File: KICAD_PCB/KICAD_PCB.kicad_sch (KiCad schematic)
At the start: 6 parts, among them J1 RPi, J2 Protoboard, U1 TPS7A0233DBVR

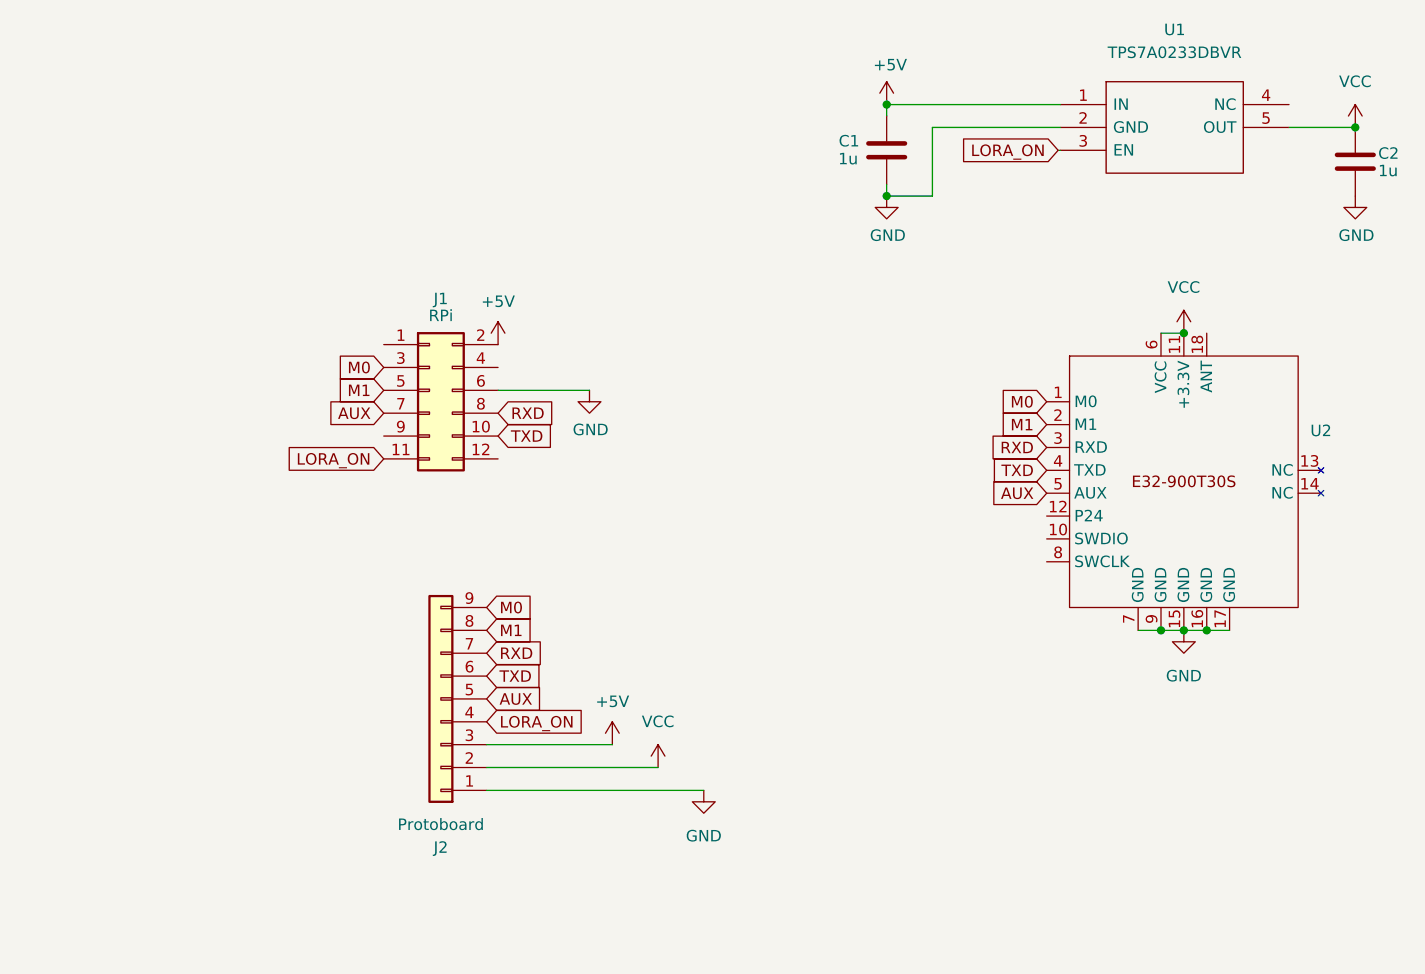
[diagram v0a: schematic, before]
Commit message: Adição do conector genérico J3
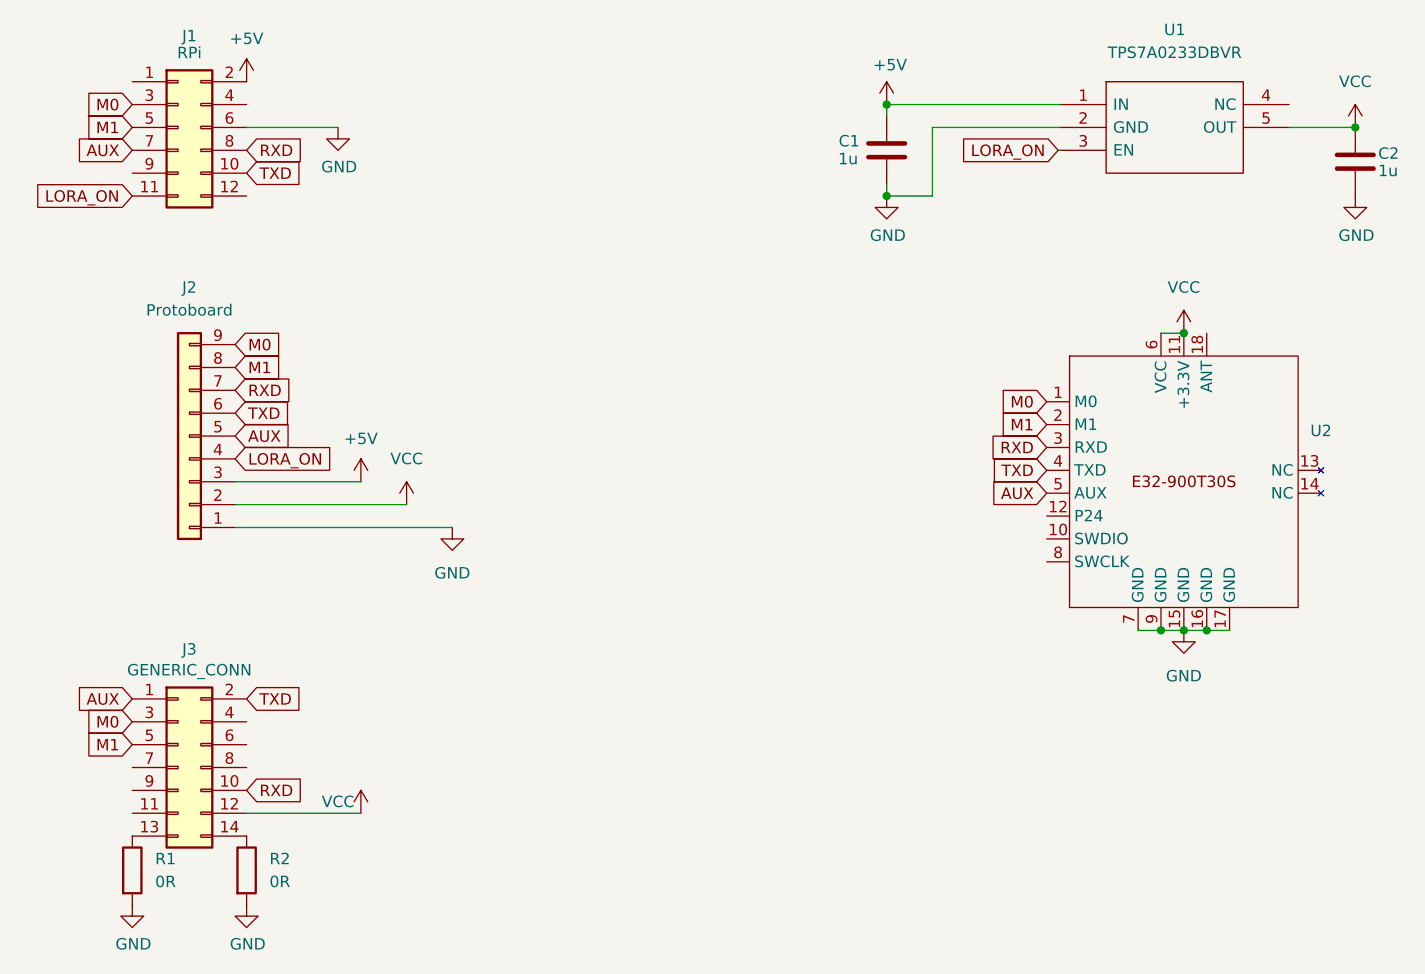
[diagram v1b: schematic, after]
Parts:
- added J3: GENERIC_CONN, Connector_PinSocket_2.54mm:PinSocket_2x07_P2.54mm_Vertical, symbol MICRO-SOP_RADIO-GENERIC-rescue:Conn_02x07_Odd_Even-Connector_Generic
- added R1, R2: 0R, Resistor_SMD:R_0805_2012Metric, symbol Device:R
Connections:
- net AUX: now also J3.1 (Pin_1)
- net GND: now also R1.2, R2.2
- net M0: now also J3.3 (Pin_3)
- net M1: now also J3.5 (Pin_5)
- net RXD: now also J3.10 (Pin_10)
- net TXD: now also J3.2 (Pin_2)
- net VCC: now also J3.12 (Pin_12)
- new net: J3.14 (Pin_14), R2.1
- new net: J3.13 (Pin_13), R1.1
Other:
- moved on the sheet: J1, J2
